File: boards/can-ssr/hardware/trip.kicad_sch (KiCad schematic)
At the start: 18 parts, among them Q20 2N7002, Q21 2N7002, Q22 2N7002, U20 LM393B

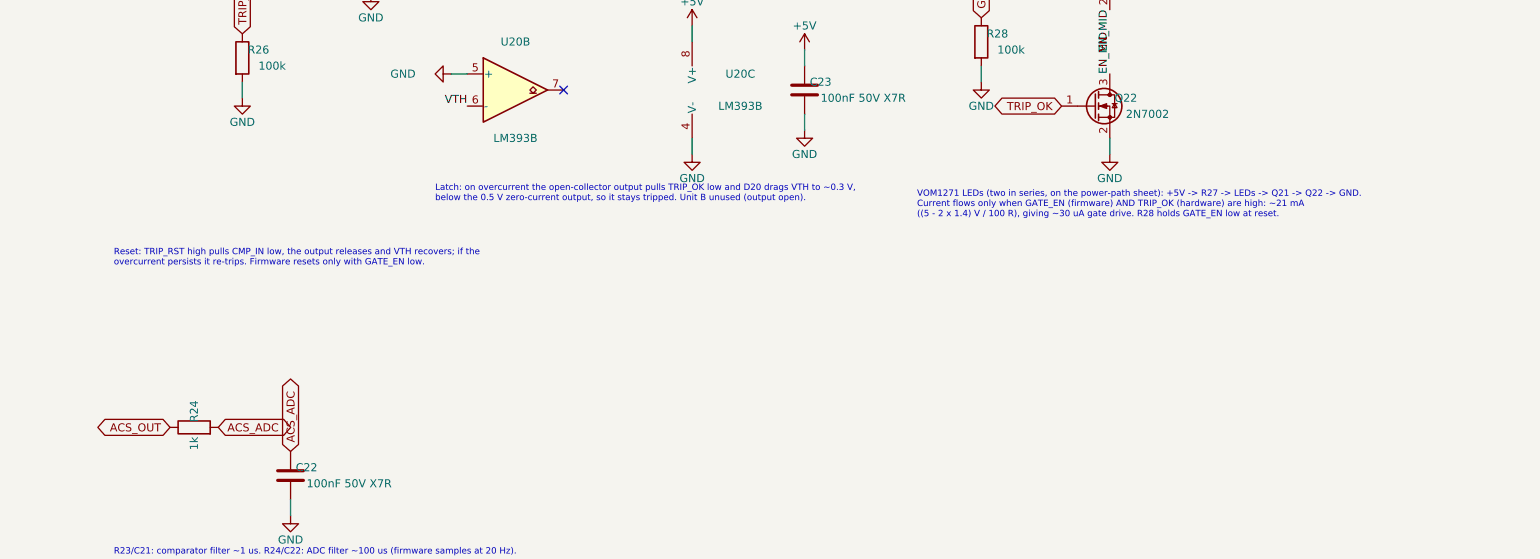
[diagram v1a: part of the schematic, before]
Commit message: can-ssr: hardware interlock holds gate drive off during trip reset
Q23 in series with the VOM1271 LED string, held on by R29 and switched
off by Q24 whenever TRIP_RST is high, so the blinded-trip window of a
latch reset can never coincide with an enabled switch.

Co-Authored-By: Claude Opus 5.5 <noreply@anthropic.com>
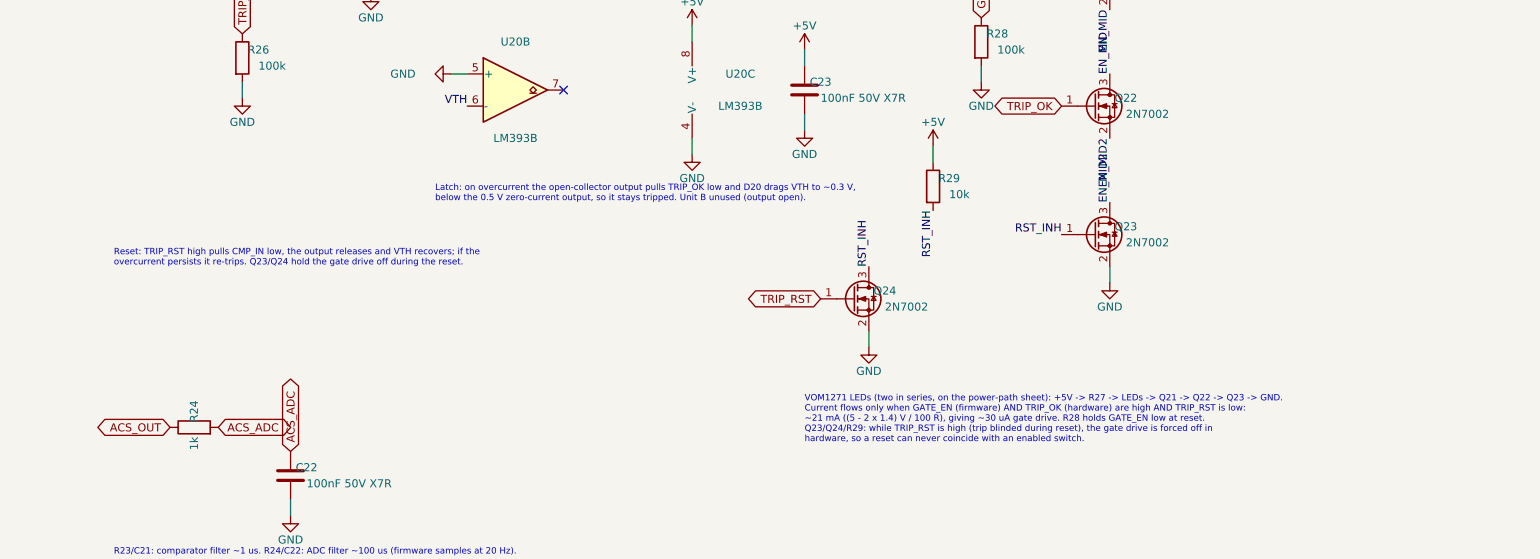
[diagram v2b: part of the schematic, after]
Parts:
- added Q23, Q24: 2N7002, Package_TO_SOT_SMD:SOT-23, symbol Transistor_FET:Q_NMOS_GSD
- added R29: 10k, Resistor_SMD:R_1206_3216Metric_Pad1.30x1.75mm_HandSolder, symbol Device:R
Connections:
- net +5V: now also R29.1
- net GND: now also Q23.2 (S), Q24.2 (S); no longer Q22.2 (S)
- net TRIP_RST: now also Q24.1 (G)
- new net EN_MID2: Q22.2 (S), Q23.3 (D)
- new net RST_INH: Q23.1 (G), Q24.3 (D), R29.2
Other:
- note added: "Reset: TRIP_RST high pulls CMP_IN low, the output releases and VTH recovers; if the overcurrent persists it re-trips. Q23/Q24 hold the gate drive off during the reset."
- note added: "VOM1271 LEDs (two in series, on the power-path sheet): +5V -> R27 -> LEDs -> Q21 -> Q22 -> Q23 -> GND. Current flows only when GATE_EN (firmware) AND TRIP_OK (hardware) are high AND TRIP_RST is low: ~21 mA ((5 - 2 x 1.4) V / 100 R), giving ~30 uA gate drive. R28 holds GATE_EN low at reset. Q23/Q24/R29: while TRIP_RST is high (trip blinded during reset), the gate drive is forced off in hardware, s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"
- note removed: "Reset: TRIP_RST high pulls CMP_IN low, the output releases and VTH recovers; if the overcurrent persists it re-trips. Firmware resets only with GATE_EN low."
- note removed: "VOM1271 LEDs (two in series, on the power-path sheet): +5V -> R27 -> LEDs -> Q21 -> Q22 -> GND. Current flows only when GATE_EN (firmware) AND TRIP_OK (hardware) are high: ~21 mA ((5 - 2 x 1.4) V / 100 R), giving ~30 uA gate drive. R28 holds GATE_EN low at reset."

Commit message: can-ssr: C21 MPN to the 1206 part (GRM3195C1H102JA01D)
The footprint is 1206; GRM2165... is an 0805 part.

Co-Authored-By: Claude Opus 5.5 <noreply@anthropic.com>
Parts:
- C21: MPN GRM2165C1H102JA01D -> GRM3195C1H102JA01D
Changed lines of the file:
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@@
 			)
 		)
-		(property "MPN" "GRM2165C1H102JA01D"
+		(property "MPN" "GRM3195C1H102JA01D"
 			(at 142.24 63.5 0)
 			(hide yes)

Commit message: Move core, can-card, io-card, serial-card, can-ssr, probe-helper to rev B
Rev A went to PCBWay and is tagged revA. Rev B replaces parts the Mouser
BOM check flagged (obsolete, end of life, not recommended for new designs,
or not orderable) and swaps out-of-stock passives and diodes for in-stock
equivalents. Field-only changes, same footprints, no layout change; the
reference boards (can-controller, pic-module) get the same part numbers.
The rev A order lists (DigiKey, Mouser) carry the same substitutions; the
Mouser list leaves out the T821 box headers (bought from DigiKey).

docs/rev-b-changes.md lists every change and the rev B to-dos (MAX7219 is
obsolete and must be replaced). transfer/mouser-revA.xlsx (Mouser BOM
check) consumed.

Co-Authored-By: Claude Opus 5.5 <noreply@anthropic.com>
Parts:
- C20, C22, C23: MPN GRM21BR71H104KA01L -> C0805C104K5RACTU; Manufacturer Murata -> KEMET
- C21: MPN GRM3195C1H102JA01D -> C1206C102J5GACTU; Manufacturer Murata -> KEMET
- D20: MPN BAT54,215 -> BAT54-7-F; Manufacturer Nexperia -> Diodes Incorporated
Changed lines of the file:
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@@
 		(title "CAN SSR: overcurrent trip and gate drive")
 		(date "2026-10-04")
-		(rev "A")
+		(rev "B")
 	)
 	(text "CAN/LOGIC SIDE. Hardware overcurrent trip, independent of firmware: the comparator latches\nand removes the VOM1271 LED current. Firmware can reset the latch (TRIP_RST) but not override it."
@@
 			)
 		)
-		(property "Manufacturer" "Murata"
+		(property "Manufacturer" "KEMET"
 			(at 66.04 81.28 0)
 			(hide yes)
@@
 			)
 		)
-		(property "MPN" "GRM21BR71H104KA01L"
+		(property "MPN" "C0805C104K5RACTU"
 			(at 66.04 81.28 0)
 			(hide yes)
@@
 			)
 		)
-		(property "Manufacturer" "Murata"
+		(property "Manufacturer" "KEMET"
 			(at 142.24 63.5 0)
 			(hide yes)
@@
 			)
 		)
-		(property "MPN" "GRM3195C1H102JA01D"
+		(property "MPN" "C1206C102J5GACTU"
 			(at 142.24 63.5 0)
 			(hide yes)
@@
 			)
 		)
-		(property "Manufacturer" "Murata"
+		(property "Manufacturer" "KEMET"
 			(at 144.78 160.02 0)
 			(hide yes)
@@
 			)
 		)
-		(property "MPN" "GRM21BR71H104KA01L"
+		(property "MPN" "C0805C104K5RACTU"
 			(at 144.78 160.02 0)
 			(hide yes)
@@
 			)
 		)
-		(property "Manufacturer" "Murata"
+		(property "Manufacturer" "KEMET"
 			(at 226.06 99.06 0)
 			(hide yes)
@@
 			)
 		)
-		(property "MPN" "GRM21BR71H104KA01L"
+		(property "MPN" "C0805C104K5RACTU"
 			(at 226.06 99.06 0)
 			(hide yes)
@@
 			)
 		)
-		(property "Manufacturer" "Nexperia"
+		(property "Manufacturer" "Diodes Incorporated"
 			(at 205.74 76.2 0)
 			(hide yes)
@@
 			)
 		)
-		(property "MPN" "BAT54,215"
+		(property "MPN" "BAT54-7-F"
 			(at 205.74 76.2 0)
 			(hide yes)
